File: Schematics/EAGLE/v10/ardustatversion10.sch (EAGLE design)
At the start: 29 parts

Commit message: Added switch and moved some wires
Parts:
- removed POT: (no value), ic-package:DIL14S
- added JP2, JP3: (no value), pinhead:PINHD-1X3
- added JP4, JP5: (no value), pinhead:PINHD-1X4
- added U$7: CD4066, ardustat:CD4066
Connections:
- new net N$23: JP3.1, JP3.3, RELAY.7
- new net N$28: JP4.2, U$7.BOUT/IN
- new net N$30: U$7.COUT/IN
- new net N$31: JP4.4, U$7.DOUT/IN
- net GND: now also U$7.VSS; no longer POT.4
- net N$11: no longer ADCS.2, POT.8, RELAY.1
- net N$15: now also ADCS.2, U$7.AIN/OUT, U$7.BIN/OUT, U$7.CIN/OUT, U$7.DIN/OUT
- net N$2: no longer POT.2
- net N$22: now also U$7.VDD
- net N$26: no longer RELAY.7
- net N$27: now also JP4.1, U$7.AOUT/IN; no longer JP1.1, U$4.-IN, U$4.VOUT
- net N$29: no longer POT.14
- net N$3: no longer POT.3
- net N$8: now also JP5.1, JP5.2, JP5.3, JP5.4, RELAY.1; no longer POT.9
- net N$9: now also JP1.1, JP2.1, JP2.2, JP2.3, U$4.-IN, U$4.VOUT; no longer J1.8, POT.1
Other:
- note added: "Test T-amp with both directions."
- moved on the sheet: RELAY, U$2

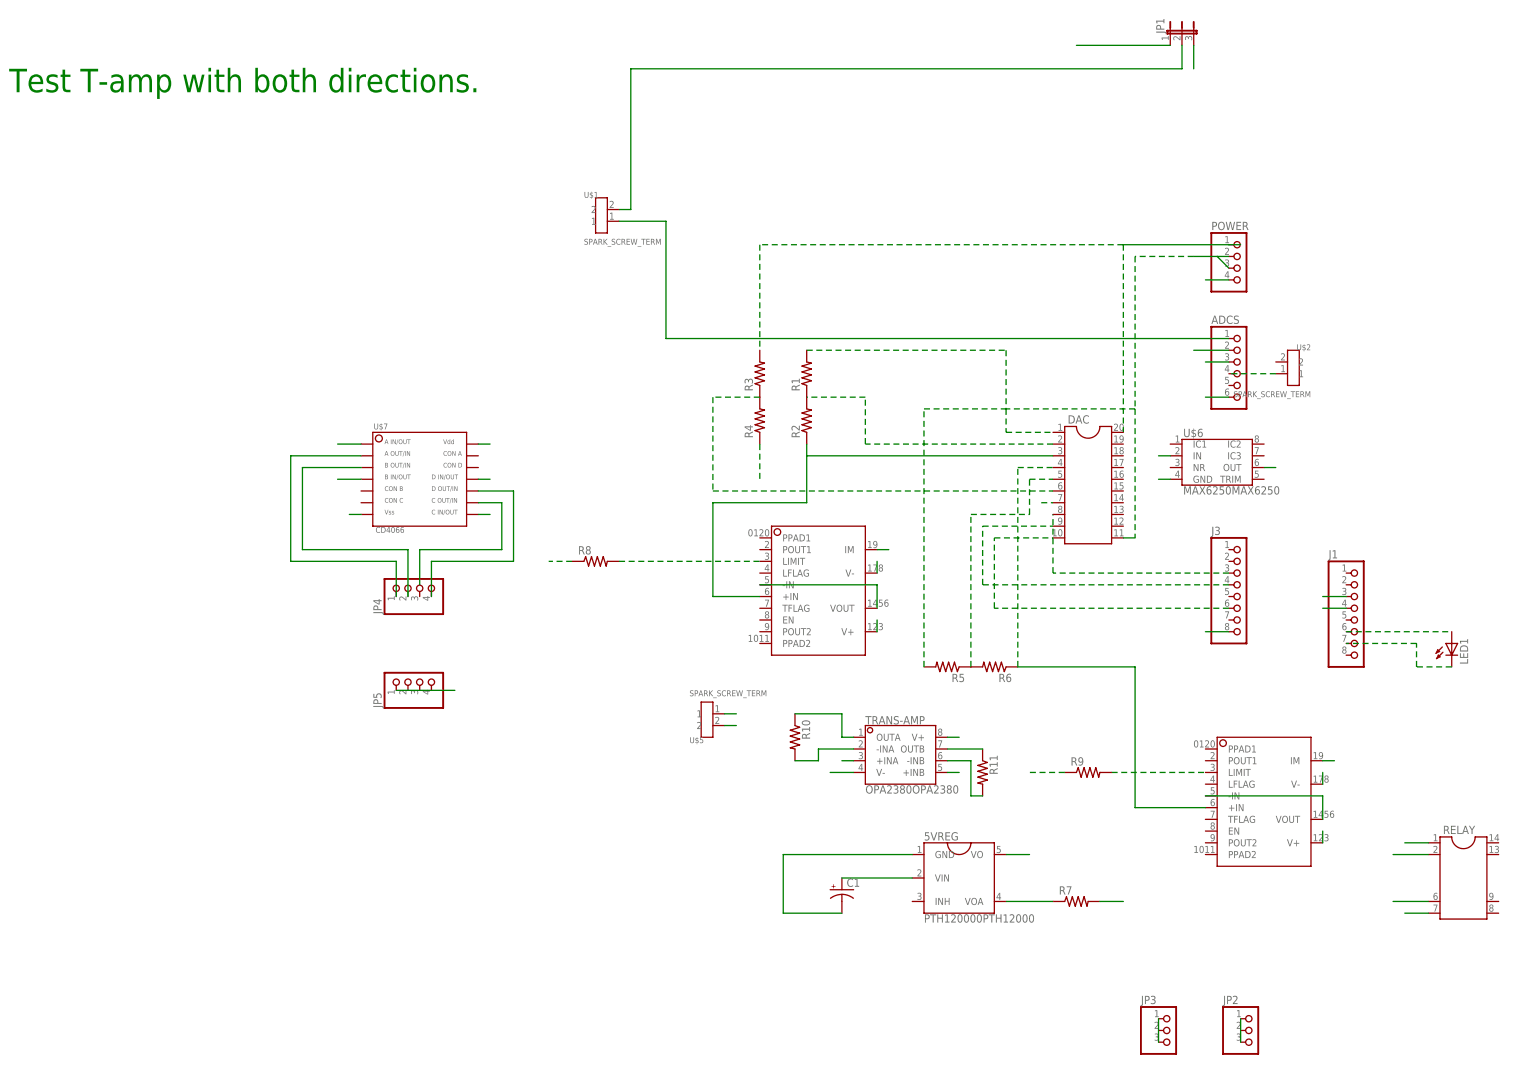
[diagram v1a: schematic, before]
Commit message: Almost finished V10 board schematic
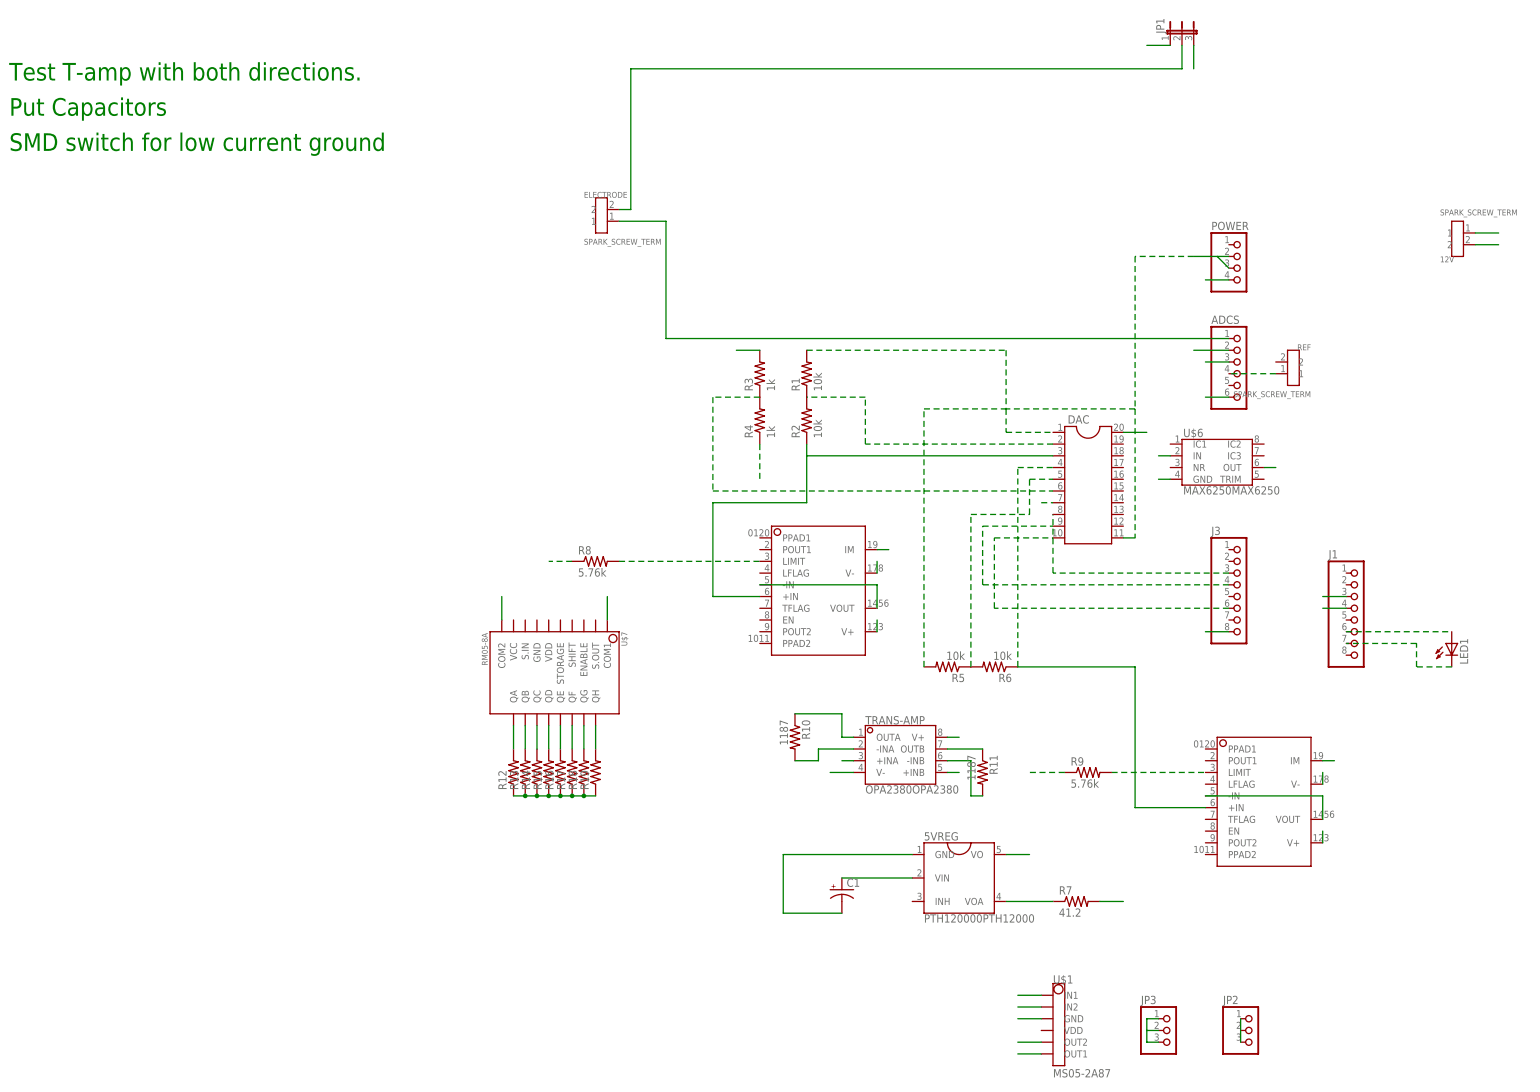
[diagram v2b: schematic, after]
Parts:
- removed JP4, JP5: (no value), pinhead:PINHD-1X4
- removed RELAY: (no value), ic-package:DIL14/8
- removed U$5: SPARK_SCREW_TERM, ardustat:SPARK_SCREW_TERM
- added 12V, ELECTRODE: SPARK_SCREW_TERM, ardustat:SPARK_SCREW_TERM
- added R12, R13, R14, R15, R16, R17, R18, R19: (no value), resistor:R-US_0207/12
- R1, R2, R5, R6: value (none) -> 10k
- R10, R11: value (none) -> 1187
- R3, R4: value (none) -> 1k
- R7: value (none) -> 41.2
- R8, R9: value (none) -> 5.76k
- U$1: value SPARK_SCREW_TERM -> MS05-2A87; device ardustat:SPARK_SCREW_TERM -> ardustat:MS05-2A87
- U$7: value CD4066 -> RM05-8A; device ardustat:CD4066 -> ardustat:RM05-8A
- renumbered U$2 to REF
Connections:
- removed net N$29: DAC.20, POWER.1, R3.2
- new net N$33: R17.2, U$7.QF
- new net N$34: R18.2, U$7.QG
- new net N$35: R19.2, U$7.QH
- new net N$36: JP1.1, U$1.OUT2
- net GND: now also 12V.2, U$1.GND; no longer RELAY.2, U$5.2, U$7.VSS
- net N$11: now also R12.2, U$7.QA; no longer TRANS-AMP.+INB
- net N$15: now also U$7.COM1, U$7.COM2; no longer U$7.AIN/OUT, U$7.BIN/OUT, U$7.CIN/OUT, U$7.DIN/OUT
- net N$19: now also DAC.20
- net N$21: now also ELECTRODE.2; no longer TRANS-AMP.+INA, U$1.2
- net N$22: now also 12V.1; no longer U$5.1, U$7.VDD
- net N$23: now also JP3.2, U$1.OUT1; no longer RELAY.7
- net N$24: now also R3.2, TRANS-AMP.+INA, TRANS-AMP.+INB
- net N$26: now also U$1.IN1
- net N$27: now also R13.2, U$7.QB; no longer JP4.1, U$7.AOUT/IN
- net N$28: now also R14.2, U$7.QC; no longer JP4.2, U$7.BOUT/IN
- net N$30: now also R15.2, U$7.QD; no longer U$7.COUT/IN
- net N$31: now also R16.2, U$7.QE; no longer JP4.4, U$7.DOUT/IN
- net N$6: no longer RELAY.6
- net N$8: now also ELECTRODE.1, JP2.1, JP2.2, JP2.3, R12.1, R13.1, R14.1, R15.1, R16.1, R17.1, R18.1, R19.1; no longer JP5.1, JP5.2, JP5.3, JP5.4, RELAY.1, U$1.1
- net N$9: now also U$1.IN2; no longer JP1.1, JP2.1, JP2.2, JP2.3
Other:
- note added: "Put Capacitors"
- note added: "SMD switch for low current ground"
